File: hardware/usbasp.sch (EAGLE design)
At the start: 25 parts, among them IC1 ATMEGA8-16A, Q2 12Mhz, X1 USB-A-H

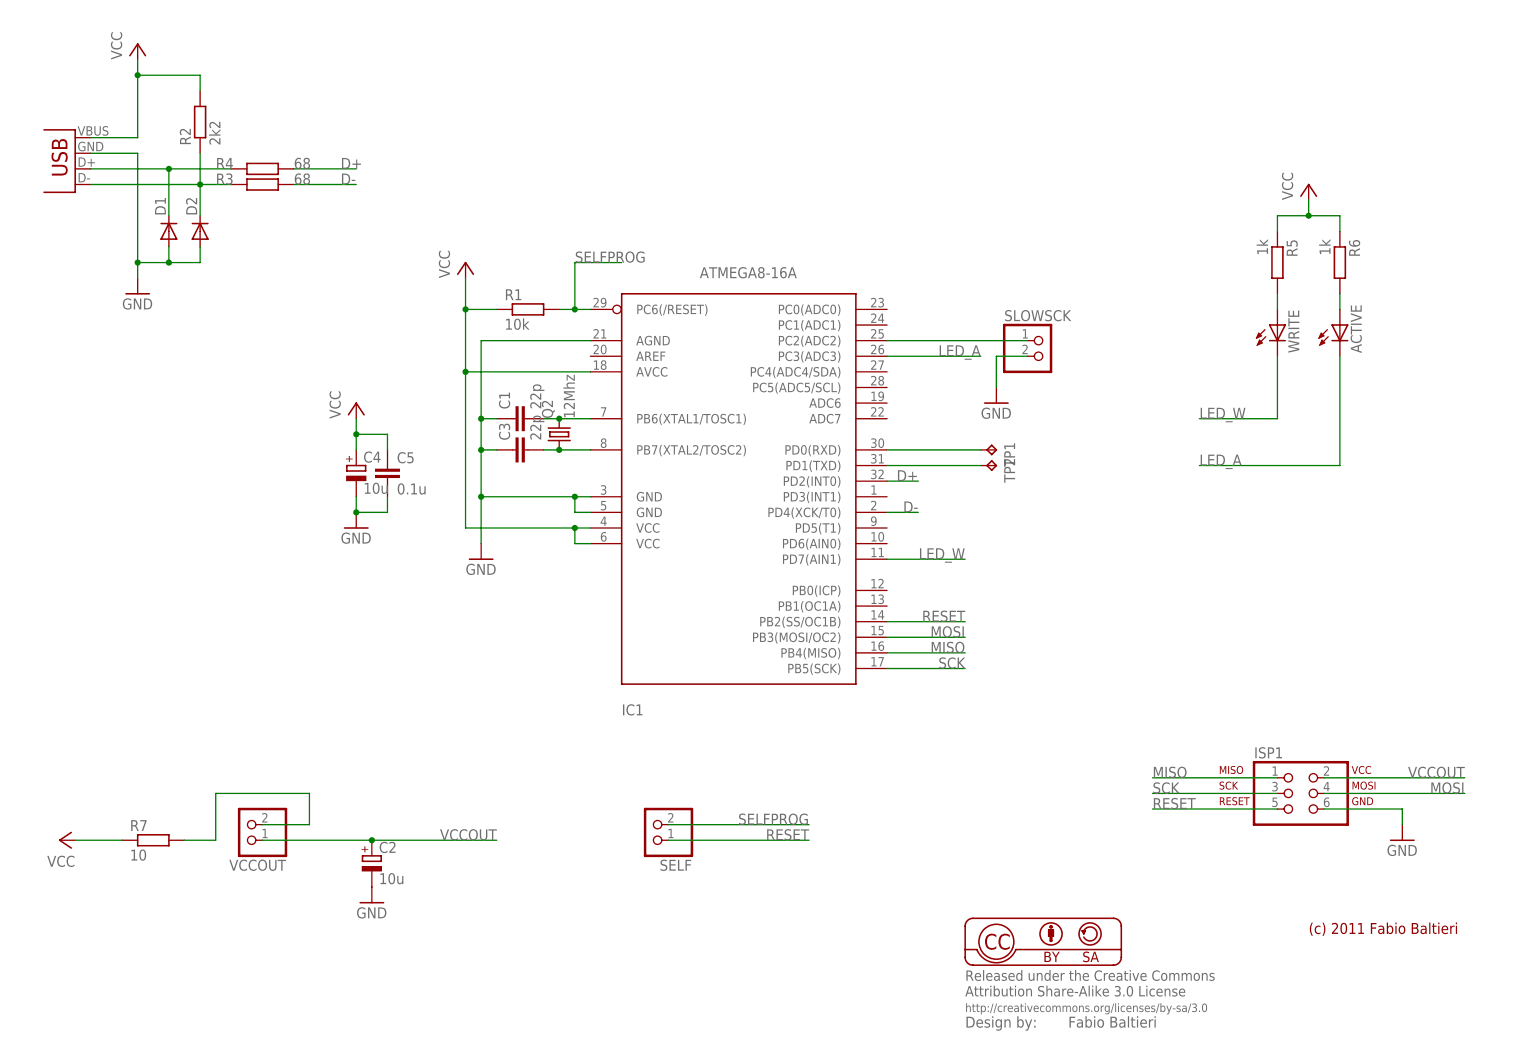
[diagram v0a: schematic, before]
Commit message: hardware: coscmetic fixes
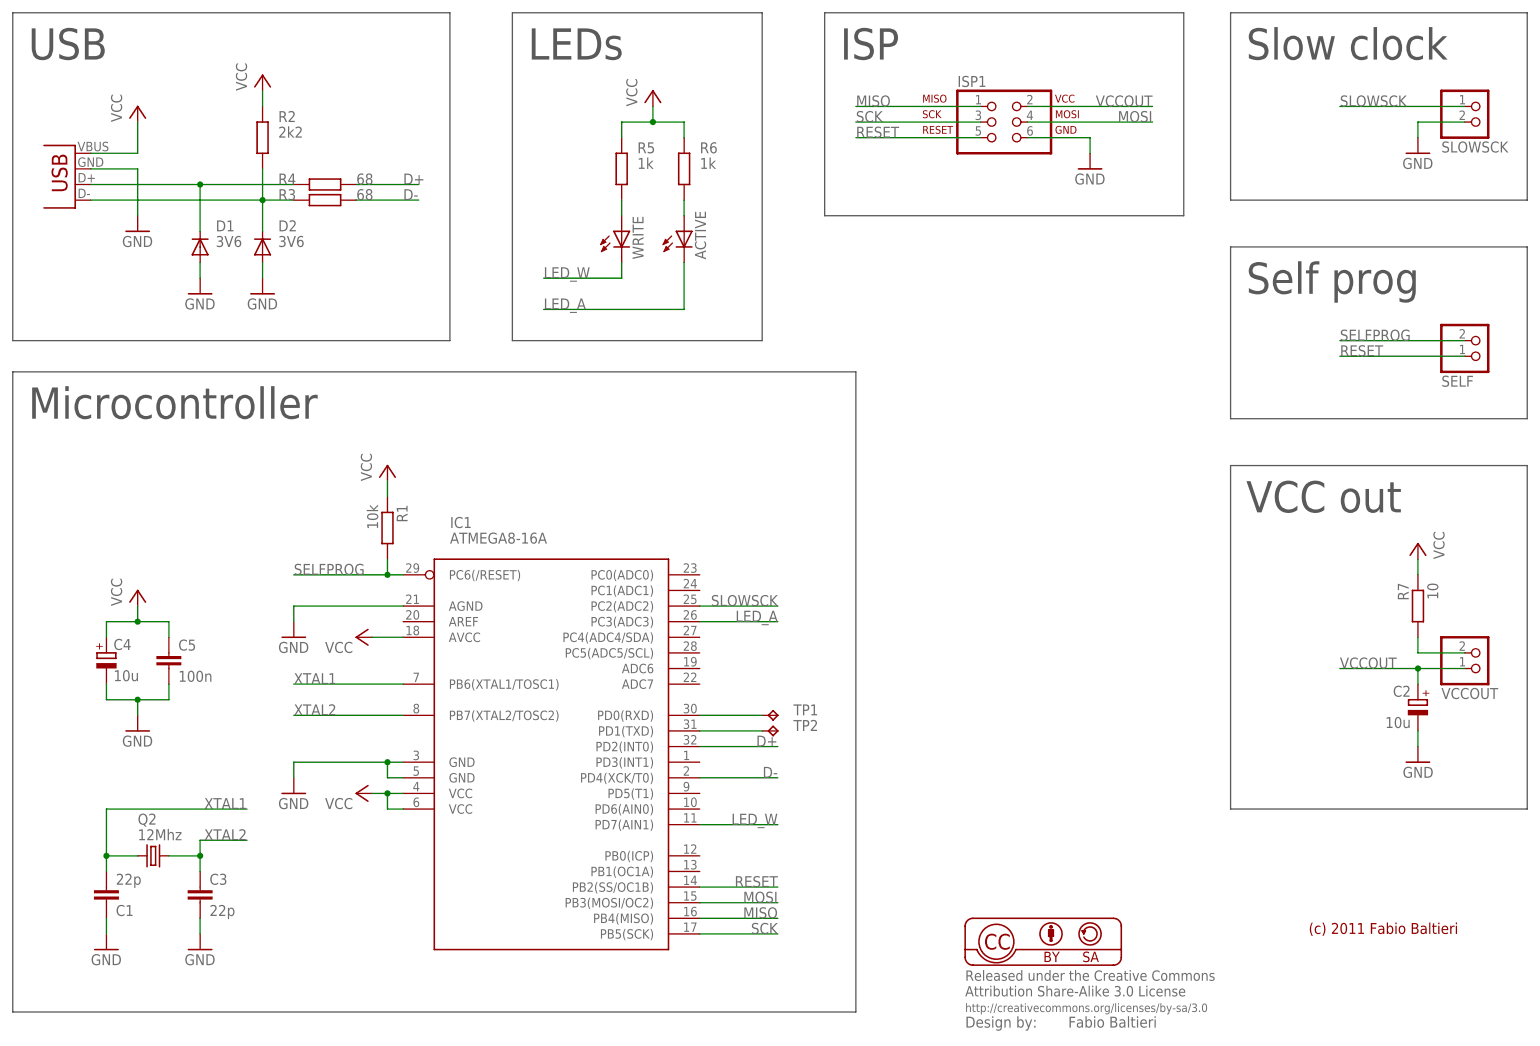
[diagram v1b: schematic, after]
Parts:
- C5: value 0.1u -> 100n
- D1, D2: value (none) -> 3V6
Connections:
- net N$1 renamed XTAL1
- net N$10 renamed SLOWSCK
- net N$2 renamed XTAL2
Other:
- note added: "ISP"
- note added: "LEDs"
- note added: "Microcontroller"
- note added: "Self prog"
- note added: "Slow clock"
- note added: "USB"
- note added: "VCC out"
- moved on the sheet: ACTIVE, C1, C2, C3, C4, C5, D1, D2, IC1, ISP1, Q2, R1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
